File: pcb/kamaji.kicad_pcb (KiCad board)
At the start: 2 copper layers, 130 x 110 mm, 34 parts, among them J1 RJ10, J2 RJ10, J3 RJ10, J4 RJ10, J5 RJ10, Q1 IRF540N, SW1 CTRL1, SW2 CTRL2, SW3 CTRL3, U1 ATMEGA328P-PU

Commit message: change a capacitor value
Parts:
- CP1: value 47uF -> 1uF
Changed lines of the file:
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@@
     (links 89)
     (no_connects 2)
-    (area 95.774999 27.55 234.275001 140.075001)
+    (area 99.924999 29.924999 230.075001 140.075001)
     (thickness 1.6)
     (drawings 7)
@@
       (effects (font (size 1 1) (thickness 0.15)))
     )
-    (fp_text value 47uF (at 0.75 3.31 270) (layer F.Fab)
-      (effects (font (size 1 1) (thickness 0.15)))
-    )
+    (fp_text value 1uF (at 0.75 3.31 270) (layer F.Fab)
+      (effects (font (size 1 1) (thickness 0.15)))
+    )

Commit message: PCB: final touches
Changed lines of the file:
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@@
     (links 89)
     (no_connects 2)
-    (area 99.924999 29.924999 230.075001 140.075001)
+    (area 88.9 21.59 243.205001 140.075001)
     (thickness 1.6)
     (drawings 7)
@@
     (visible_elements FFFFFF7F)
     (pcbplotparams
-      (layerselection 0x010f0_80000001)
-      (usegerberextensions false)
+      (layerselection 0x00020_00000000)
+      (usegerberextensions true)
       (excludeedgelayer true)
       (linewidth 0.100000)
@@
   (module kamaji:RJ10 (layer F.Cu)
     (at 205 28 180)
-    (fp_text reference J1 (at 0 -2.54 180) (layer F.SilkS)
+    (fp_text reference J1 (at -0.105 -5.02 180) (layer F.SilkS)
       (effects (font (size 1 1) (thickness 0.15)))
     )
@@
   (module kamaji:RJ10 (layer F.Cu)
     (at 185 28 180)
-    (fp_text reference J2 (at 0 -2.54 180) (layer F.SilkS)
+    (fp_text reference J2 (at 0.215 -5.02 180) (layer F.SilkS)
       (effects (font (size 1 1) (thickness 0.15)))
     )
@@
   (module kamaji:RJ10 (layer F.Cu)
     (at 165 28 180)
-    (fp_text reference J3 (at 0 -2.54 180) (layer F.SilkS)
+    (fp_text reference J3 (at -0.1 -5.02 180) (layer F.SilkS)
       (effects (font (size 1 1) (thickness 0.15)))
     )
@@
   (module kamaji:RJ10 (layer F.Cu)
     (at 145 28 180)
-    (fp_text reference J4 (at 0 -2.54 180) (layer F.SilkS)
+    (fp_text reference J4 (at 0.22 -5.02 180) (layer F.SilkS)
       (effects (font (size 1 1) (thickness 0.15)))
     )
@@
   (module kamaji:RJ10 (layer F.Cu)
     (at 125 28 180)
-    (fp_text reference J5 (at 0 -2.54 180) (layer F.SilkS)
+    (fp_text reference J5 (at -0.095 -5.02 180) (layer F.SilkS)
       (effects (font (size 1 1) (thickness 0.15)))
     )
@@
     (descr "USB B connector")
     (tags "USB_B USB_DEV")
-    (fp_text reference USB_IN1 (at 11.05 1.27 90) (layer F.SilkS)
+    (fp_text reference USB_IN1 (at 7.26 1.305 90) (layer F.SilkS)
       (effects (font (size 1 1) (thickness 0.15)))
     )
@@
     (effects (font (size 1 1) (thickness 0.15)) (justify mirror))
   )
-  (gr_text "Kamaji 1.0\nIlya Strukov <iley@iley.ru>" (at 217.8 80.7 90) (layer F.SilkS)
-    (effects (font (size 1.5 1.5) (thickness 0.3)))
+  (gr_text "Kamaji 1.0\nIlya Strukov <iley@iley.ru>" (at 163.195 115.57) (layer F.SilkS)
+    (effects (font (size 1.8 1.8) (thickness 0.3)))
   )
   (gr_line (start 230 30) (end 230 140) (angle 90) (layer Edge.Cuts) (width 0.15))
@@
       )
     )
+  )
+  (zone (net 0) (net_name "") (layer F.Mask) (hatch edge 0.508)
+    (connect_pads (clearance 0.508))
+    (min_thickness 0.254)
+    (fill yes (arc_segments 16) (thermal_gap 0.508) (thermal_bridge_width 0.508))
+    (polygon
+      (pts
+        (xy 100.965 99.06) (xy 100.965 31.115) (xy 228.6 31.115) (xy 228.6 62.23) (xy 243.205 62.23)
+        (xy 243.205 21.59) (xy 89.535 21.59) (xy 88.9 99.695) (xy 100.965 99.695)
+      )
+    )

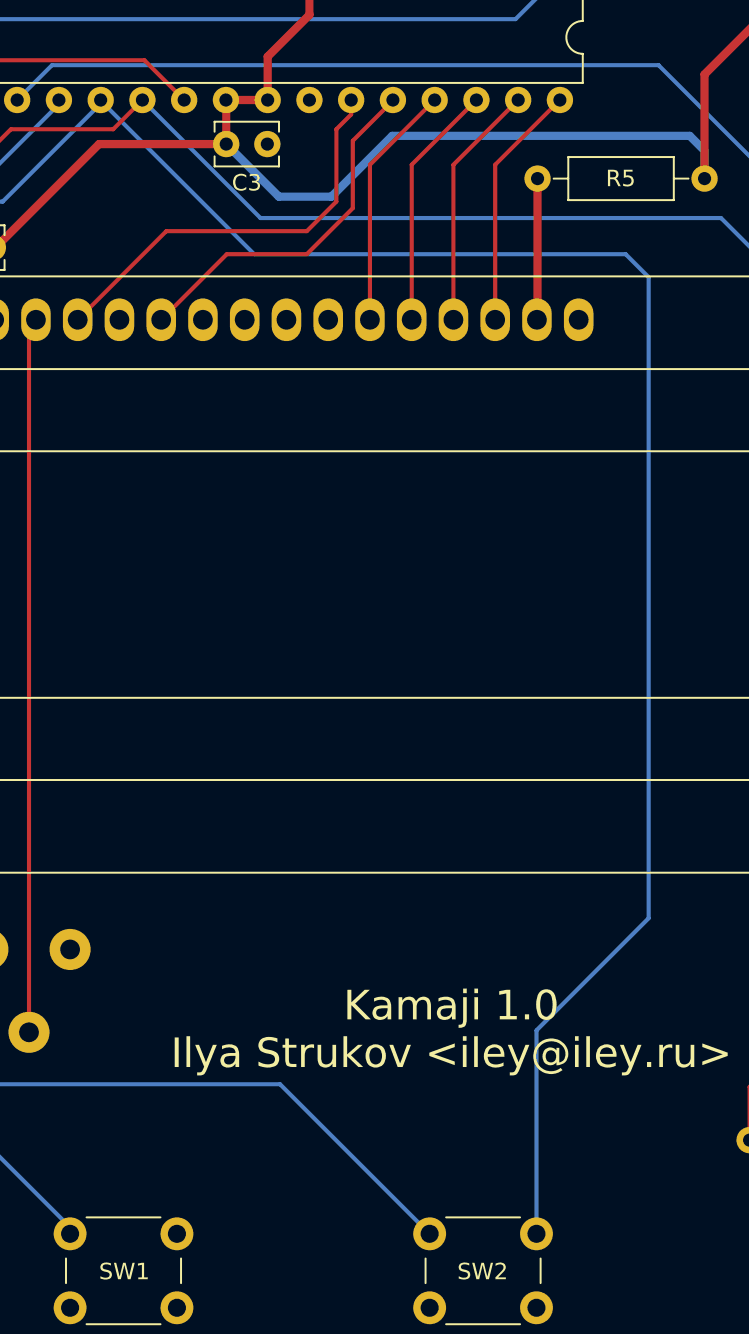
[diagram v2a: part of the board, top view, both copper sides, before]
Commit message: remove the extra trace going to one of the buttons
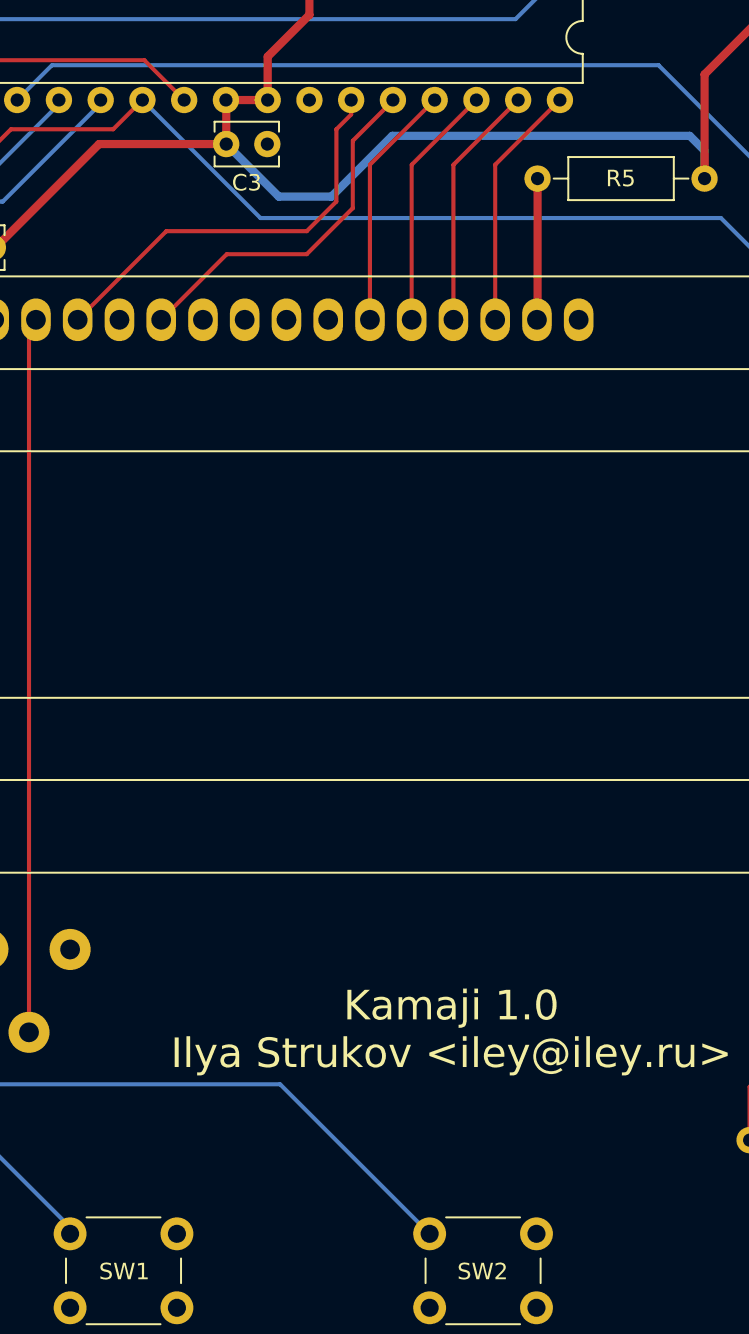
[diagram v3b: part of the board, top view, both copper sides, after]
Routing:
- net CBTN2: track 227.2 -> 128.4 mm
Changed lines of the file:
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@@
   (general
     (links 89)
-    (no_connects 2)
+    (no_connects 3)
     (area 88.9 21.59 243.205001 140.075001)
     (thickness 1.6)
     (drawings 7)
-    (tracks 177)
+    (tracks 171)
     (zones 0)
     (modules 34)
@@
   (segment (start 135.9 65.2) (end 127.8 65.2) (width 0.25) (layer B.Cu) (net 20))
   (segment (start 141.86 59.02) (end 141.86 59.06) (width 0.25) (layer B.Cu) (net 20))
-  (segment (start 141.86 59.06) (end 151.2 68.4) (width 0.25) (layer B.Cu) (net 20))
-  (segment (start 151.2 68.4) (end 173.8 68.4) (width 0.25) (layer B.Cu) (net 20))
-  (segment (start 173.8 68.4) (end 175.2 69.8) (width 0.25) (layer B.Cu) (net 20))
-  (segment (start 175.2 69.8) (end 175.2 108.8) (width 0.25) (layer B.Cu) (net 20))
-  (segment (start 175.2 108.8) (end 168.375 115.625) (width 0.25) (layer B.Cu) (net 20))
-  (segment (start 168.375 115.625) (end 168.375 128) (width 0.25) (layer B.Cu) (net 20))
   (segment (start 110.8 63.78) (end 123.82 63.78) (width 0.25) (layer F.Cu) (net 21))
   (segment (start 167.1 54.1) (end 169.8 51.4) (width 0.25) (layer B.Cu) (net 21))

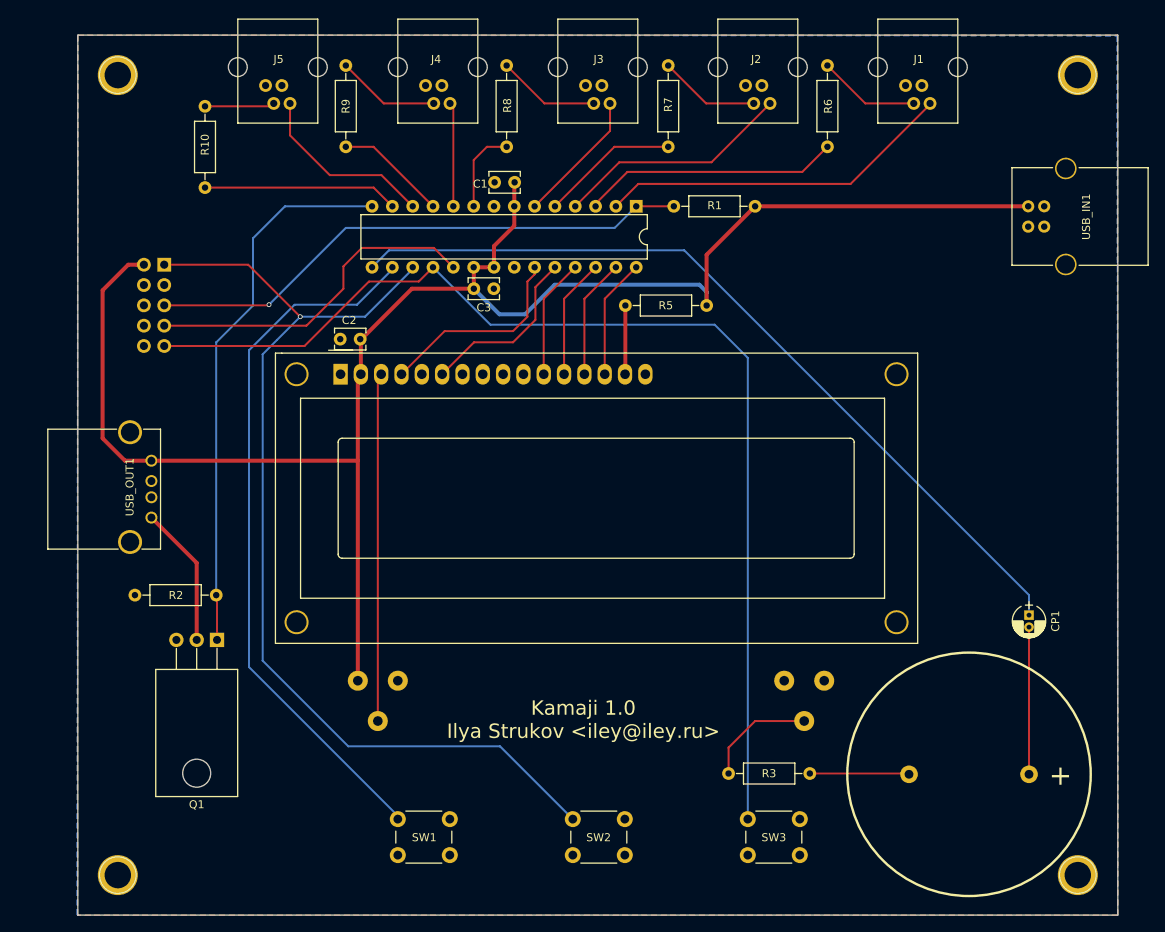
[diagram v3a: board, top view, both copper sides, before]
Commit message: start laying out a new, smaller PCB
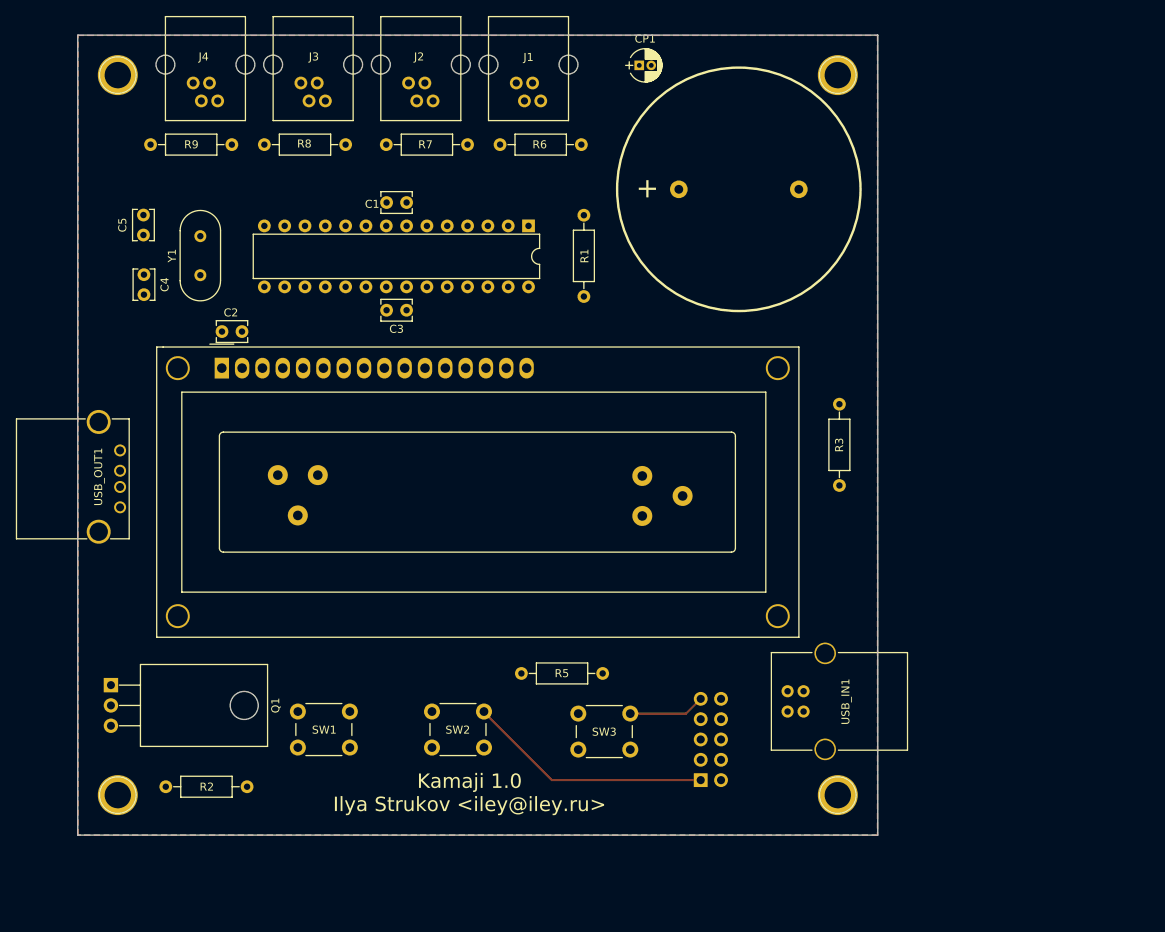
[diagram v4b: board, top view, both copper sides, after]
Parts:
- removed J5: RJ10, kamaji:RJ10
- removed R10: 220R, Resistors_THT:R_Axial_DIN0207_L6.3mm_D2.5mm_P10.16mm_Horizontal
- added C4: C, Capacitors_THT:C_Disc_D3.8mm_W2.6mm_P2.50mm, F.Cu at (108.3, 59.9)
- added C5: C, Capacitors_THT:C_Disc_D3.8mm_W2.6mm_P2.50mm, F.Cu at (108.2, 55.0)
- added Y1: Crystal, Crystals:Crystal_HC49-U_Vertical, F.Cu at (115.3, 60.0)
- moved JP1 93.0 mm to (177.9, 123.1), turned to 90 degrees
- moved CP1 84.2 mm to (170.2, 33.8), turned to 0 degrees
- moved LS1 78.6 mm to (182.6, 49.3), turned to 0 degrees
- moved USB_IN1 67.7 mm to (188.7, 112.0)
- moved J1 48.7 mm to (156.3, 27.7)
- moved R5 47.8 mm to (165.6, 109.8)
- moved R3 46.3 mm to (195.2, 76.1), turned to 270 degrees
- moved J2 42.1 mm to (142.9, 27.7)
- moved R6 42.1 mm to (152.8, 43.7), turned to 0 degrees
- moved R7 36.6 mm to (138.6, 43.7), turned to 0 degrees
- moved J3 35.6 mm to (129.4, 27.7)
- moved R8 31.9 mm to (123.3, 43.7), turned to 0 degrees
- moved REF** 31.6 mm to (195.0, 125.0)
- moved REF** 30.0 mm to (195.0, 35.0)
- moved J4 29.1 mm to (116.0, 27.7)
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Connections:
- U1 pad 10: PBTN4 -> XTAL2
- U1 pad 11: PLED4 -> PLED3
- U1 pad 12: PBTN5 -> PBTN4
- U1 pad 13: PLED5 -> PLED4
- U1 pad 9: PLED3 -> XTAL1
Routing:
- net VCC: track 218.9 -> 0.00 mm
- net CBTN3: track 139.5 -> 9.57 mm
- net SND: track 103.4 -> 0.00 mm
- net CBTN2: track 128.4 -> 30.7 mm, vias 1 -> 0
- net CBTN1: track 89.1 -> 0.00 mm
- net RST: track 68.8 -> 0.00 mm, vias 1 -> 0
- net LAMP: track 68.7 -> 0.00 mm
- net PBTN1: track 44.7 -> 0.00 mm
- net Net-(DS1-Pad3): track 44.7 -> 0.00 mm
- net SCK: track 42.9 -> 0.00 mm
- net PLED1: track 32.2 -> 0.00 mm
- net PBTN2: track 29.7 -> 0.00 mm
- net LCD_RS: track 25.3 -> 0.00 mm
- net PLED5: track 24.4 -> 0.00 mm
- net PBTN5: track 23.0 -> 0.00 mm
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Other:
- board size 130 x 110 mm -> 100 x 100 mm

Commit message: lay out the 1.1 PCB
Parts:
- moved Y1 4.31 mm to (114.3, 55.8)
- moved C4 4.26 mm to (108.4, 55.7)
- moved C5 4.08 mm to (108.5, 50.9)
- moved CP1 3.84 mm to (166.8, 35.6)
- moved USB_OUT1 2.72 mm to (108.0, 82.0)
- moved SW2 0.85 mm to (145.0, 115.0)
- moved SW1 0.66 mm to (128.0, 115.0)
- moved SW3 0.59 mm to (162.0, 115.0)
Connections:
- U1 pad 16: CBTN1 -> LCD_RS
- U1 pad 2: PBTN1 -> PLED1
- U1 pad 23: LCD_RS -> CBTN1
- U1 pad 3: PLED1 -> PBTN1
- U1 pad 4: PBTN2 -> PLED2
- U1 pad 5: PLED2 -> PBTN2
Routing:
- net VCC: track 0.00 -> 188.3 mm
- net RST: track 0.00 -> 111.9 mm
- net CBTN3: track 9.57 -> 113.3 mm
- net LAMP: track 0.00 -> 93.5 mm
- net CBTN2: track 30.7 -> 124.2 mm
- net SCK: track 0.00 -> 93.1 mm
- net CBTN1: track 0.00 -> 83.8 mm
- net SND: track 0.00 -> 64.9 mm
- net XTAL1: track 0.00 -> 39.2 mm
- net Net-(DS1-Pad15): track 0.00 -> 38.9 mm
- net Net-(Q1-Pad2): track 0.00 -> 29.7 mm
- net Net-(LS1-Pad2): track 0.00 -> 29.0 mm
- net XTAL2: track 0.00 -> 26.2 mm
- net PBTN3: track 0.00 -> 24.0 mm
- net LCD_EN: track 0.00 -> 22.6 mm
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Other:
- board text added: "Kamaji 1.1 Ilya Strukov <iley@iley.ru>"
- board text removed: "Kamaji 1.0 Ilya Strukov <iley@iley.ru>"

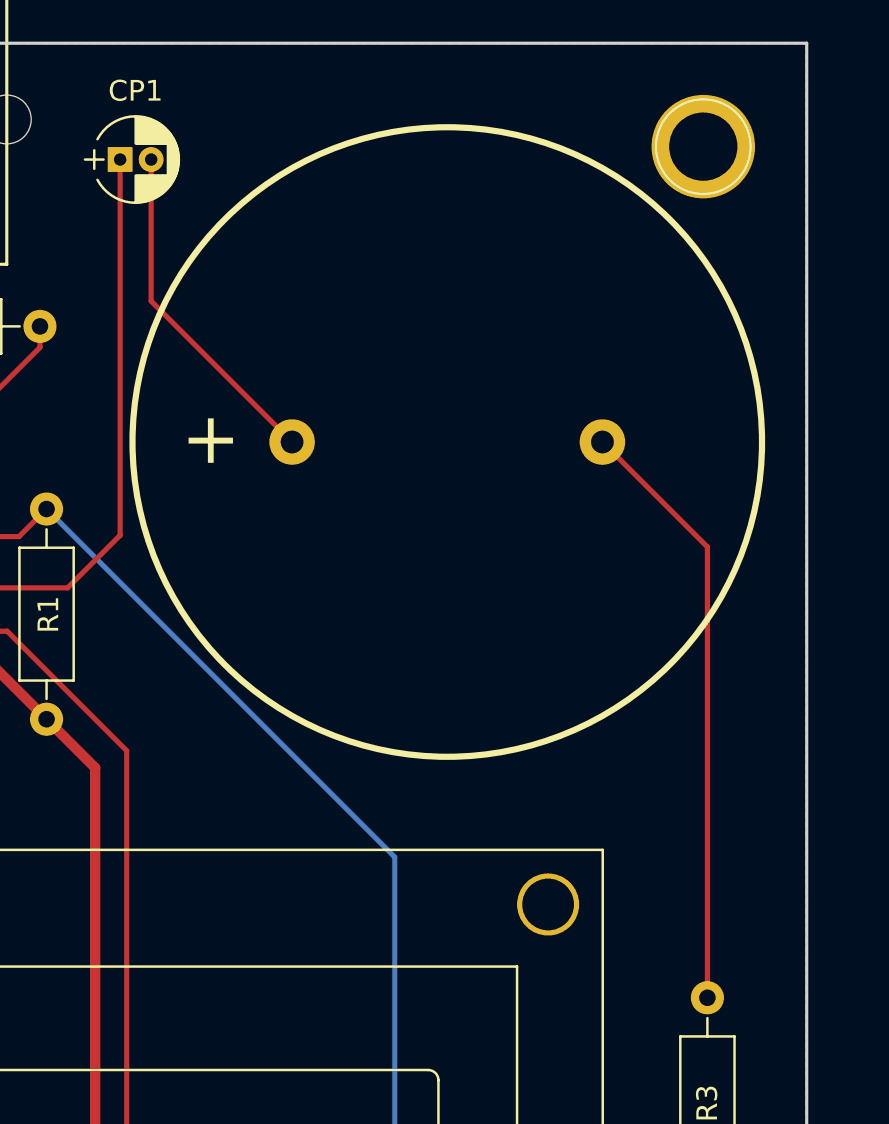
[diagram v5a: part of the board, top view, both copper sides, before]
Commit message: move the speaker footprint
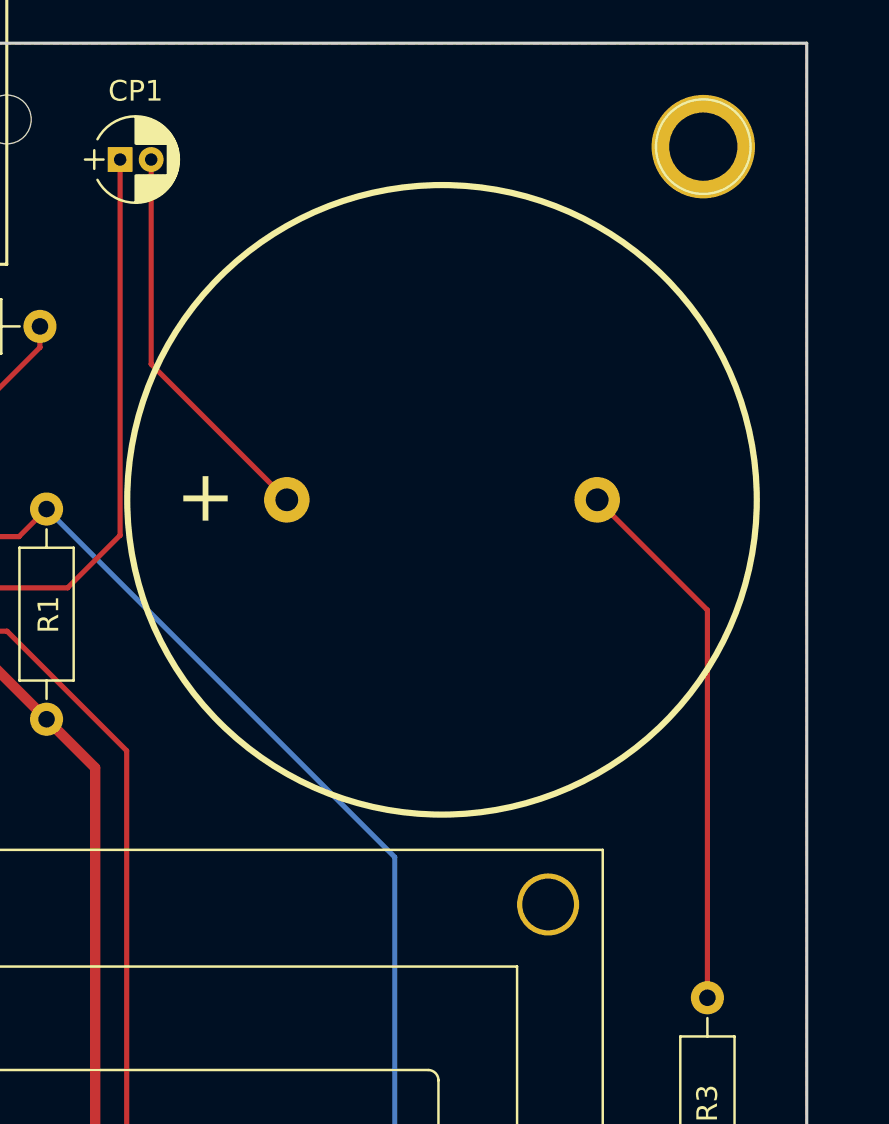
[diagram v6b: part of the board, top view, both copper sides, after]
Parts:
- moved LS1 2.81 mm to (182.4, 52.1)
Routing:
- net Net-(CP1-Pad2): track 16.5 -> 19.2 mm
- net Net-(LS1-Pad2): track 29.0 -> 26.3 mm
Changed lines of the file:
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@@
     (links 90)
     (no_connects 0)
-    (area 99.924999 29.924999 200.075001 130.075001)
+    (area 94.574999 27.236 204.197001 130.075001)
     (thickness 1.6)
     (drawings 7)
@@
   )
   (module kamaji:AL-30P (layer F.Cu)
-    (at 182.626 49.276)
+    (at 182.372 52.07)
     (fp_text reference LS1 (at 0.036 0.02) (layer F.SilkS) hide
       (effects (font (size 1 1) (thickness 0.15)))
@@
   (segment (start 156.337 53.848) (end 161.925 53.848) (width 0.25) (layer F.Cu) (net 19))
   (segment (start 161.925 53.848) (end 163.2585 52.5145) (width 0.25) (layer F.Cu) (net 19))
-  (segment (start 195.199 76.1365) (end 195.199 54.349) (width 0.25) (layer F.Cu) (net 20))
-  (segment (start 195.199 54.349) (end 190.126 49.276) (width 0.25) (layer F.Cu) (net 20))
+  (segment (start 195.199 76.1365) (end 195.199 57.397) (width 0.25) (layer F.Cu) (net 20) (status 400000))
+  (segment (start 195.199 57.397) (end 189.872 52.07) (width 0.25) (layer F.Cu) (net 20) (status 800000))
   (segment (start 123.317 61.468) (end 123.444 61.468) (width 0.25) (layer F.Cu) (net 21))
   (segment (start 123.444 61.468) (end 128.5875 56.3245) (width 0.25) (layer F.Cu) (net 21))
@@
   (segment (start 175.601 87.6065) (end 193.889 87.6065) (width 0.25) (layer F.Cu) (net 31))
   (segment (start 193.889 87.6065) (end 195.199 86.2965) (width 0.25) (layer F.Cu) (net 31))
-  (segment (start 168.3145 35.6235) (end 168.3145 42.4645) (width 0.25) (layer F.Cu) (net 41))
-  (segment (start 168.3145 42.4645) (end 175.126 49.276) (width 0.25) (layer F.Cu) (net 41))
+  (segment (start 168.3145 35.6235) (end 168.3145 45.5125) (width 0.25) (layer F.Cu) (net 41) (status 400000))
+  (segment (start 168.3145 45.5125) (end 174.872 52.07) (width 0.25) (layer F.Cu) (net 41) (status 800000))
   (segment (start 152.781 43.688) (end 152.781 41.272) (width 0.25) (layer F.Cu) (net 43))
   (segment (start 152.781 41.272) (end 155.827 38.226) (width 0.25) (layer F.Cu) (net 43))
